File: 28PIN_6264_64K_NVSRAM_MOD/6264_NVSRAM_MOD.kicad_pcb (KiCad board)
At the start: 2 copper layers, 17.8 x 35.6 mm, 18 parts, among them J1 Conn_01x02, U1 TL431DBZ, U10 TC5564APL_Adapter, U2 74AHC2G00, U3 STK12C68

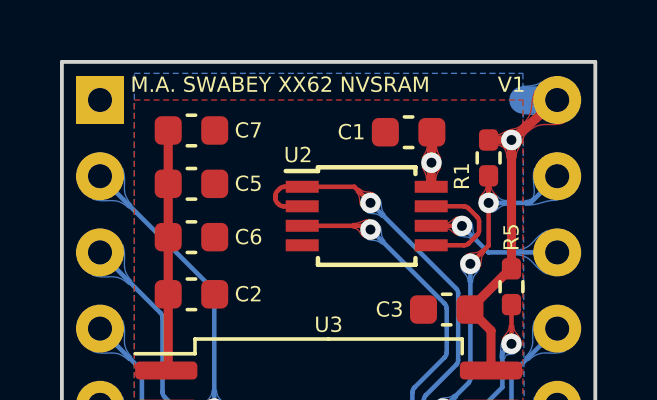
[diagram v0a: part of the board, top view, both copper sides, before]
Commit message: Updated silkscreen w. new naming scheme.
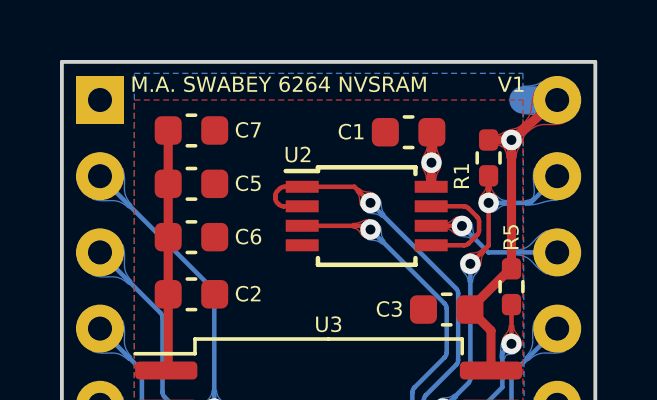
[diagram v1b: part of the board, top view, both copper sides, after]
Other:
- board text added: "M.A. SWABEY 6264 NVSRAM"
- board text removed: "M.A. SWABEY XX62 NVSRAM"
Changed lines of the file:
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@@
     (descr "SOIC, 28 Pin (https://www.infineon.com/dgdl/Infineon-STK12C68_64_Kbit_(8_K_x_8)_AutoStore_nvSRAM_Datasheet-AdditionalTechnicalInformation-v09_00-EN.pdf?fileId=8ac78c8c7d0d8da4017d0ecc045f45bf#page=16), generated with kicad-footprint-generator ipc_gullwing_generator.py")
     (tags "SOIC SO")
-    (property "Sheetfile" "XX62_NVSRAM_MOD.kicad_sch")
+    (property "Sheetfile" "6264_NVSRAM_MOD.kicad_sch")
     (property "Sheetname" "")
     (attr smd)
@@
     (descr "TSSOP8: plastic thin shrink small outline package; 8 leads; body width 3 mm; (see NXP SSOP-TSSOP-VSO-REFLOW.pdf and sot505-1_po.pdf)")
     (tags "SSOP 0.65")
-    (property "Sheetfile" "XX62_NVSRAM_MOD.kicad_sch")
+    (property "Sheetfile" "6264_NVSRAM_MOD.kicad_sch")
     (property "Sheetname" "")
     (attr smd)
@@
     (descr "Resistor SMD 0402 (1005 Metric), square (rectangular) end terminal, IPC_7351 nominal with elongated pad for handsoldering. (Body size source: IPC-SM-782 page 72, https://www.pcb-3d.com/wordpress/wp-content/uploads/ipc-sm-782a_amendment_1_and_2.pdf), generated with kicad-footprint-generator")
     (tags "resistor handsolder")
-    (property "Sheetfile" "XX62_NVSRAM_MOD.kicad_sch")
+    (property "Sheetfile" "6264_NVSRAM_MOD.kicad_sch")
     (property "Sheetname" "")
     (attr smd)
@@
     (descr "Resistor SMD 0402 (1005 Metric), square (rectangular) end terminal, IPC_7351 nominal with elongated pad for handsoldering. (Body size source: IPC-SM-782 page 72, https://www.pcb-3d.com/wordpress/wp-content/uploads/ipc-sm-782a_amendment_1_and_2.pdf), generated with kicad-footprint-generator")
     (tags "resistor handsolder")
-    (property "Sheetfile" "XX62_NVSRAM_MOD.kicad_sch")
+    (property "Sheetfile" "6264_NVSRAM_MOD.kicad_sch")
     (property "Sheetname" "")
     (attr smd)
@@
     (tags "connector JST PH side entry")
     (property "MPN" "XX62 nvSRAM V1")
-    (property "Sheetfile" "XX62_NVSRAM_MOD.kicad_sch")
+    (property "Sheetfile" "6264_NVSRAM_MOD.kicad_sch")
     (property "Sheetname" "")
     (attr through_hole)
@@
     (property "Digikey" "1276-1111-2-ND")
     (property "MPN" "CC0603ZRY5V8BB104")
-    (property "Sheetfile" "XX62_NVSRAM_MOD.kicad_sch")
+    (property "Sheetfile" "6264_NVSRAM_MOD.kicad_sch")
     (property "Sheetname" "")
     (attr smd)
@@
     (descr "Resistor SMD 0402 (1005 Metric), square (rectangular) end terminal, IPC_7351 nominal with elongated pad for handsoldering. (Body size source: IPC-SM-782 page 72, https://www.pcb-3d.com/wordpress/wp-content/uploads/ipc-sm-782a_amendment_1_and_2.pdf), generated with kicad-footprint-generator")
     (tags "resistor handsolder")
-    (property "Sheetfile" "XX62_NVSRAM_MOD.kicad_sch")
+    (property "Sheetfile" "6264_NVSRAM_MOD.kicad_sch")
     (property "Sheetname" "")
     (attr smd)
@@
     (property "Digikey" "ZTL431AFCT-ND")
     (property "MPN" "ZTL431AFTA")
-    (property "Sheetfile" "XX62_NVSRAM_MOD.kicad_sch")
+    (property "Sheetfile" "6264_NVSRAM_MOD.kicad_sch")
     (property "Sheetname" "")
     (attr smd)
@@
     (descr "Resistor SMD 0402 (1005 Metric), square (rectangular) end terminal, IPC_7351 nominal with elongated pad for handsoldering. (Body size source: IPC-SM-782 page 72, https://www.pcb-3d.com/wordpress/wp-content/uploads/ipc-sm-782a_amendment_1_and_2.pdf), generated with kicad-footprint-generator")
     (tags "resistor handsolder")
-    (property "Sheetfile" "XX62_NVSRAM_MOD.kicad_sch")
+    (property "Sheetfile" "6264_NVSRAM_MOD.kicad_sch")
     (property "Sheetname" "")
     (attr smd)
@@
     (descr "28-lead though-hole mounted DIP package, row spacing 15.24 mm (600 mils), Socket")
     (tags "THT DIP DIL PDIP 2.54mm 15.24mm 600mil Socket")
-    (property "Sheetfile" "XX62_NVSRAM_MOD.kicad_sch")
+    (property "Sheetfile" "6264_NVSRAM_MOD.kicad_sch")
     (property "Sheetname" "")
     (attr through_hole)
@@
     (property "Digikey" "1276-1274-2-ND")
     (property "MPN" "CL10A226MP8NUNE")
-    (property "Sheetfile" "XX62_NVSRAM_MOD.kicad_sch")
+    (property "Sheetfile" "6264_NVSRAM_MOD.kicad_sch")
     (property "Sheetname" "")
     (attr smd)
@@
     (property "Digikey" "1276-1274-2-ND")
     (property "MPN" "CL10A226MP8NUNE")
-    (property "Sheetfile" "XX62_NVSRAM_MOD.kicad_sch")
+    (property "Sheetfile" "6264_NVSRAM_MOD.kicad_sch")
     (property "Sheetname" "")
     (attr smd)
@@
     (property "Digikey" "1276-1274-2-ND")
     (property "MPN" "CL10A226MP8NUNE")
-    (property "Sheetfile" "XX62_NVSRAM_MOD.kicad_sch")
+    (property "Sheetfile" "6264_NVSRAM_MOD.kicad_sch")
     (property "Sheetname" "")
     (attr smd)
@@
     (property "Digikey" "1276-1111-2-ND")
     (property "MPN" "CC0603ZRY5V8BB104")
-    (property "Sheetfile" "XX62_NVSRAM_MOD.kicad_sch")
+    (property "Sheetfile" "6264_NVSRAM_MOD.kicad_sch")
     (property "Sheetname" "")
     (attr smd)
@@
     (property "Digikey" "1276-1274-2-ND")
     (property "MPN" "CL10A226MP8NUNE")
-    (property "Sheetfile" "XX62_NVSRAM_MOD.kicad_sch")
+    (property "Sheetfile" "6264_NVSRAM_MOD.kicad_sch")
     (property "Sheetname" "")
     (attr smd)
@@
     (descr "Resistor SMD 0402 (1005 Metric), square (rectangular) end terminal, IPC_7351 nominal with elongated pad for handsoldering. (Body size source: IPC-SM-782 page 72, https://www.pcb-3d.com/wordpress/wp-content/uploads/ipc-sm-782a_amendment_1_and_2.pdf), generated with kicad-footprint-generator")
     (tags "resistor handsolder")
-    (property "Sheetfile" "XX62_NVSRAM_MOD.kicad_sch")
+    (property "Sheetfile" "6264_NVSRAM_MOD.kicad_sch")
     (property "Sheetname" "")
     (attr smd)
@@
     (property "Digikey" "1276-1111-2-ND")
     (property "MPN" "CC0603ZRY5V8BB104")
-    (property "Sheetfile" "XX62_NVSRAM_MOD.kicad_sch")
+    (property "Sheetfile" "6264_NVSRAM_MOD.kicad_sch")
     (property "Sheetname" "")
     (attr smd)
@@
     (descr "Resistor SMD 0402 (1005 Metric), square (rectangular) end terminal, IPC_7351 nominal with elongated pad for handsoldering. (Body size source: IPC-SM-782 page 72, https://www.pcb-3d.com/wordpress/wp-content/uploads/ipc-sm-782a_amendment_1_and_2.pdf), generated with kicad-footprint-generator")
     (tags "resistor handsolder")
-    (property "Sheetfile" "XX62_NVSRAM_MOD.kicad_sch")
+    (property "Sheetfile" "6264_NVSRAM_MOD.kicad_sch")
     (property "Sheetname" "")
     (attr smd)
@@
   (gr_line (start 128.27 57.15) (end 128.27 92.71) (layer "Edge.Cuts") (width 0.127))
   (gr_line (start 110.49 57.15) (end 128.27 57.15) (layer "Edge.Cuts") (width 0.127))
-  (gr_text "M.A. SWABEY XX62 NVSRAM" (at 112.776 57.912) (layer "F.SilkS")
+  (gr_text "M.A. SWABEY 6264 NVSRAM" (at 112.776 57.912) (layer "F.SilkS")
     (effects (font (size 0.508 0.508) (thickness 0.127)) (justify left))
   )
